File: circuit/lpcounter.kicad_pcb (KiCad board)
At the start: 2 copper layers, 58.4 x 40.6 mm, 17 parts, among them IC1 ATTINY85V-P, M1 SYN115, P1 CONN_01X08

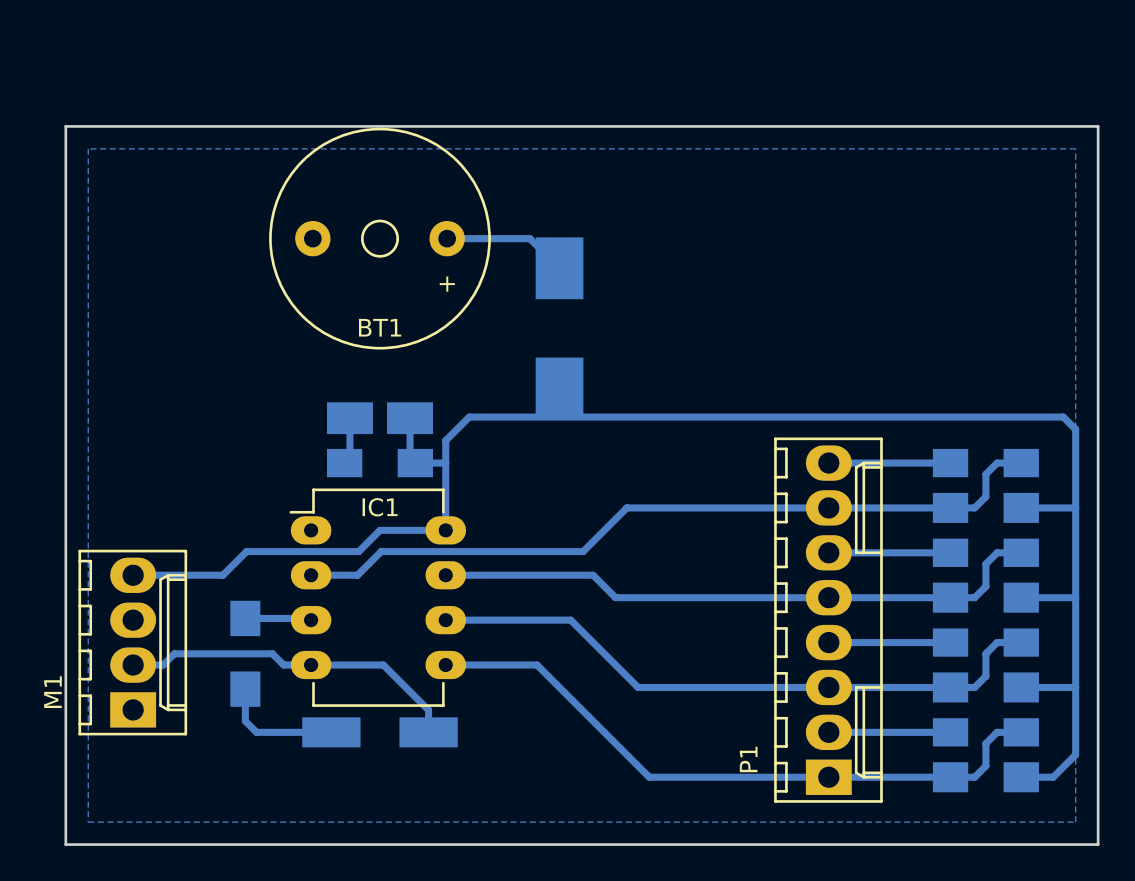
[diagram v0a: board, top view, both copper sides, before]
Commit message: proper battery holder for CR2032
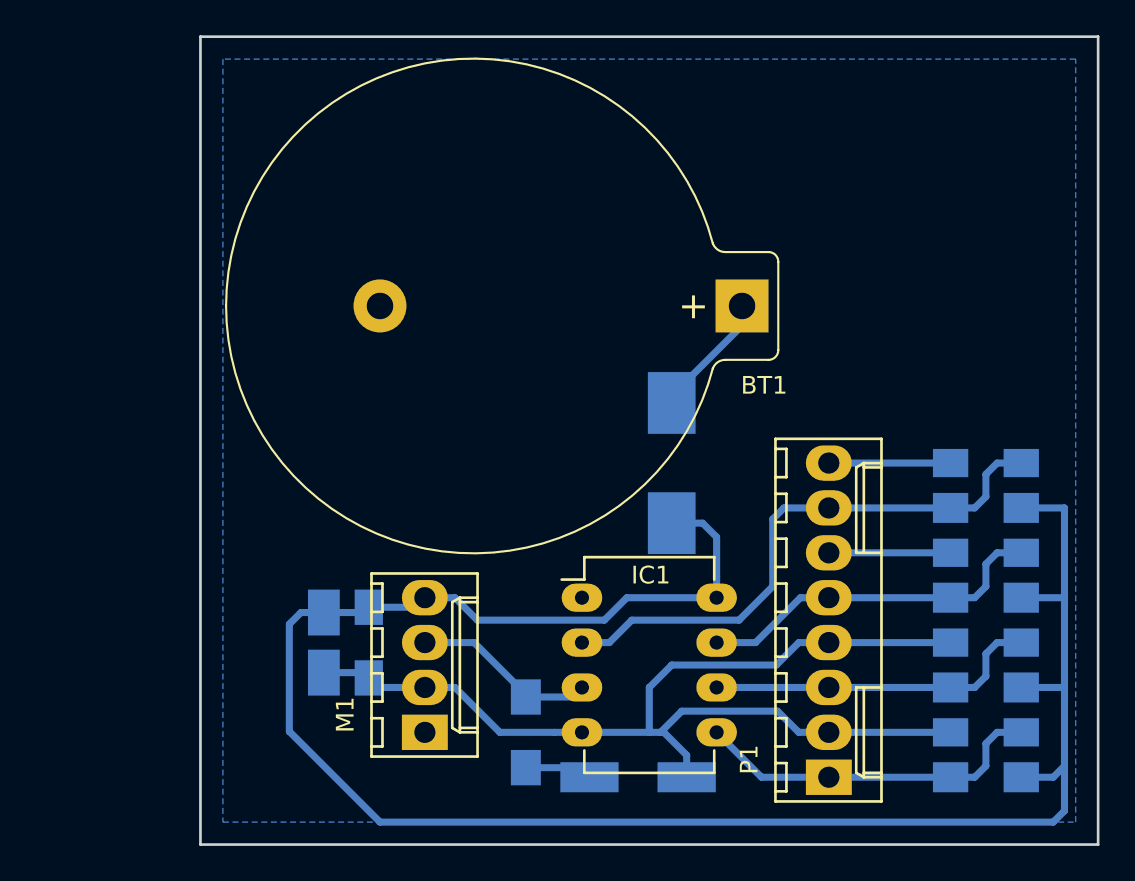
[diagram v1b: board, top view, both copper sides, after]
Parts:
- BT1: footprint Buzzers_Beepers:Buzzer_12x9.5RM7.6 -> Battery_Holders:Keystone_106_1x20mm-CoinCell
- moved BT1 20.8 mm to (172.9, 35.6)
- moved M1 16.6 mm to (154.9, 59.7)
- moved R5 16.5 mm to (160.7, 59.7)
- moved IC1 15.8 mm to (163.8, 52.1)
- moved D2 14.8 mm to (167.0, 62.2)
- moved C5 13.1 mm to (149.2, 54.6), turned to 270 degrees
- moved C6 10.2 mm to (151.8, 54.6), turned to 270 degrees
- moved D1 9.92 mm to (168.9, 44.5)
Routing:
- net GND: track 49.8 -> 75.5 mm
- net /IN0: track 37.0 -> 20.1 mm
- net /IN1: track 35.9 -> 19.0 mm
- net +3V3: track 96.0 -> 112.1 mm
- net /IN2: track 34.9 -> 20.1 mm
- net /IN3: track 43.6 -> 32.0 mm
- net /OUT: track 3.76 -> 10.5 mm
- net /LED: track 6.94 -> 3.82 mm
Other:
- board size 58.4 x 40.6 mm -> 50.8 x 45.7 mm

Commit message: updating PCB
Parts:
- M1: footprint Connectors_Molex:Molex_KK-6410-04_04x2.54mm_Straight -> Pin_Headers:Pin_Header_Straight_1x04_Pitch2.00mm
- moved M1 1.08 mm to (154.9, 58.6), turned to 180 degrees
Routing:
- net +3V3: track 112.1 -> 111.4 mm

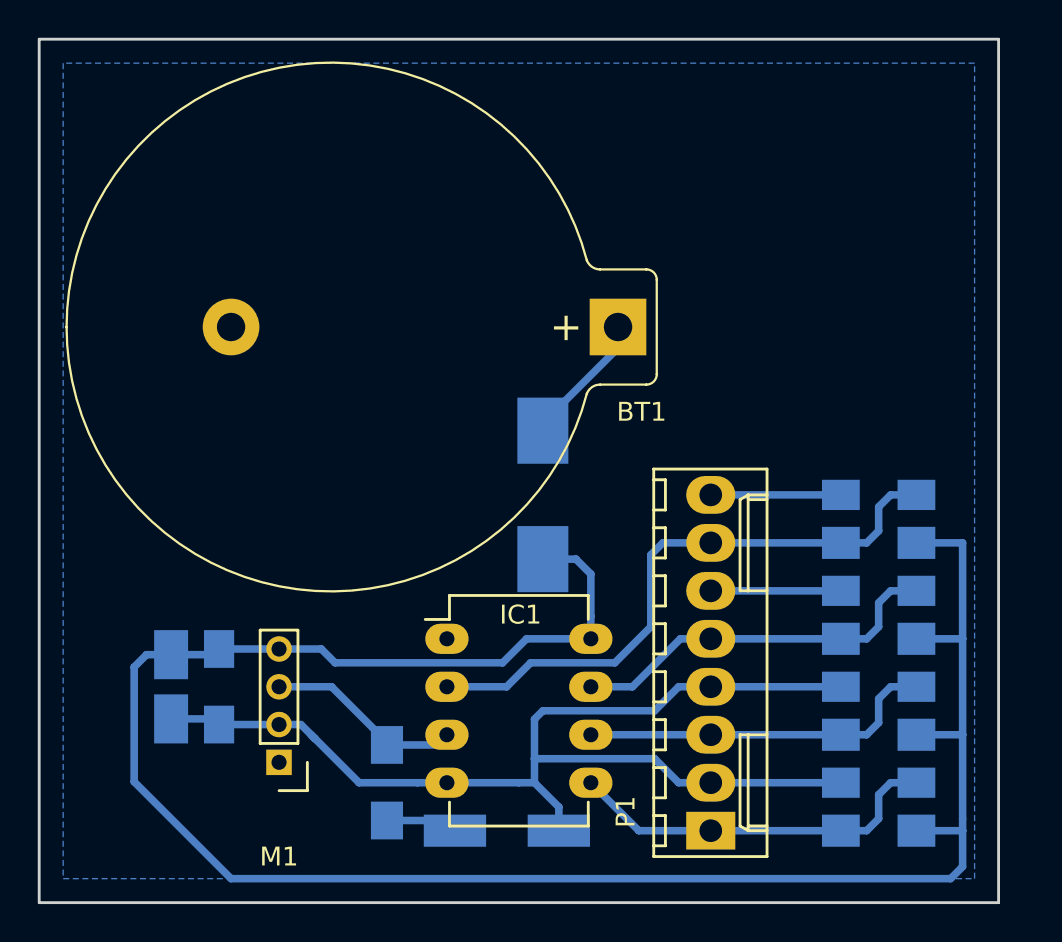
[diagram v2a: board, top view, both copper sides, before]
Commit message: fully routed
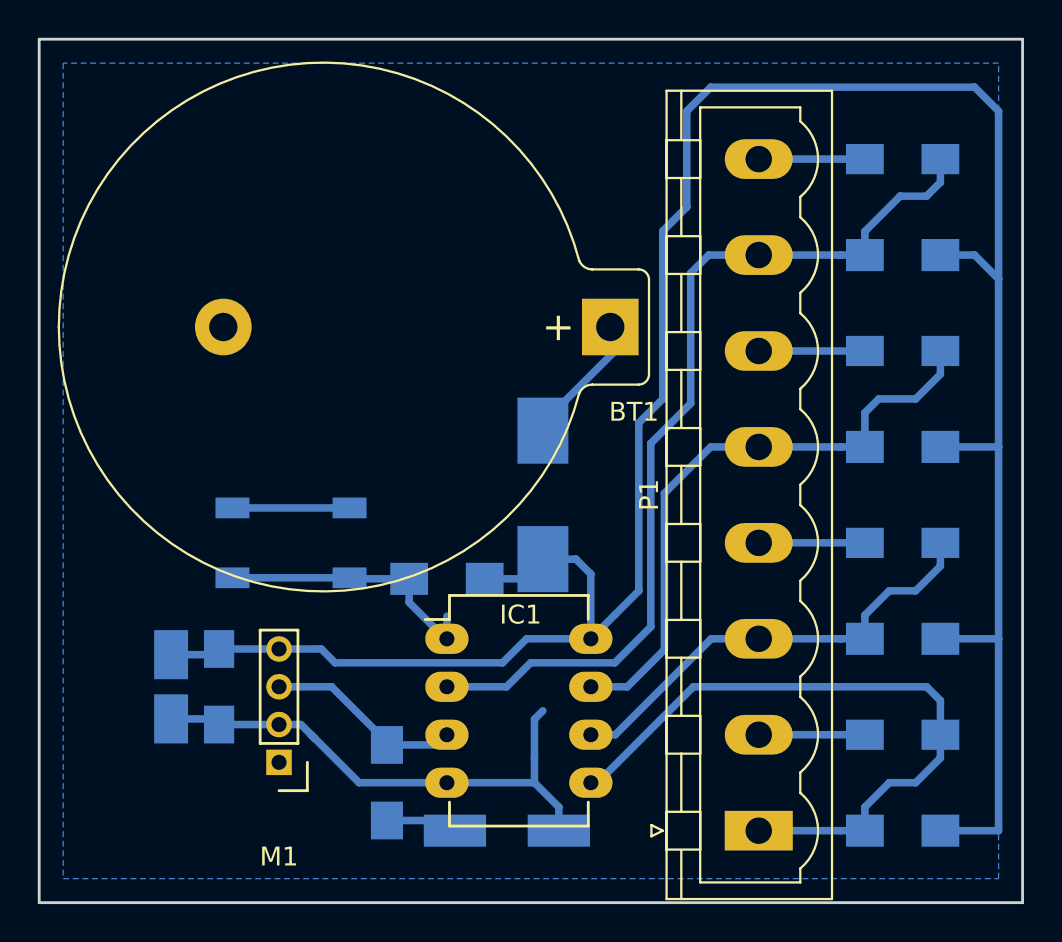
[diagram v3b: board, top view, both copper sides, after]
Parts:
- added P2: CONN_02X01, Buttons_Switches_SMD:SW_SPST_SKQG, B.Cu at (155.6, 47.0)
- added R6: 10k, Resistors_SMD:R_1206_HandSoldering, B.Cu at (163.8, 48.9)
- P1: footprint Connectors_Molex:Molex_KK-6410-08_08x2.54mm_Straight -> Connectors_Phoenix:PhoenixContact_MSTBVA-G_08x5.08mm_Vertical
- moved C4 17.8 mm to (188.0, 26.7)
- moved R4 15.3 mm to (188.0, 31.8)
- moved C3 12.8 mm to (188.0, 36.8)
- moved R3 10.2 mm to (188.0, 41.9)
- moved C2 7.73 mm to (188.0, 47.0)
- moved R2 5.24 mm to (188.0, 52.1)
- moved C1 2.84 mm to (188.0, 57.1)
- moved P1 2.54 mm to (180.3, 62.2)
- moved R1 1.27 mm to (188.0, 62.2)
- moved BT1 0.41 mm to (172.5, 35.6)
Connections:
- IC1 pad 1: (no net) -> /RESETn
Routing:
- net +3V3: track 111.4 -> 131.9 mm
- net GND: track 75.6 -> 57.4 mm
- net /IN3: track 32.0 -> 49.0 mm
- net /IN0: track 20.1 -> 36.1 mm
- net /RESETn: track 0.00 -> 14.6 mm
- net /IN2: track 20.1 -> 32.7 mm
- net /IN1: track 19.0 -> 24.3 mm
- net Net-(BT1-Pad1): track 7.14 -> 7.86 mm
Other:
- board size 50.8 x 45.7 mm -> 52.1 x 45.7 mm

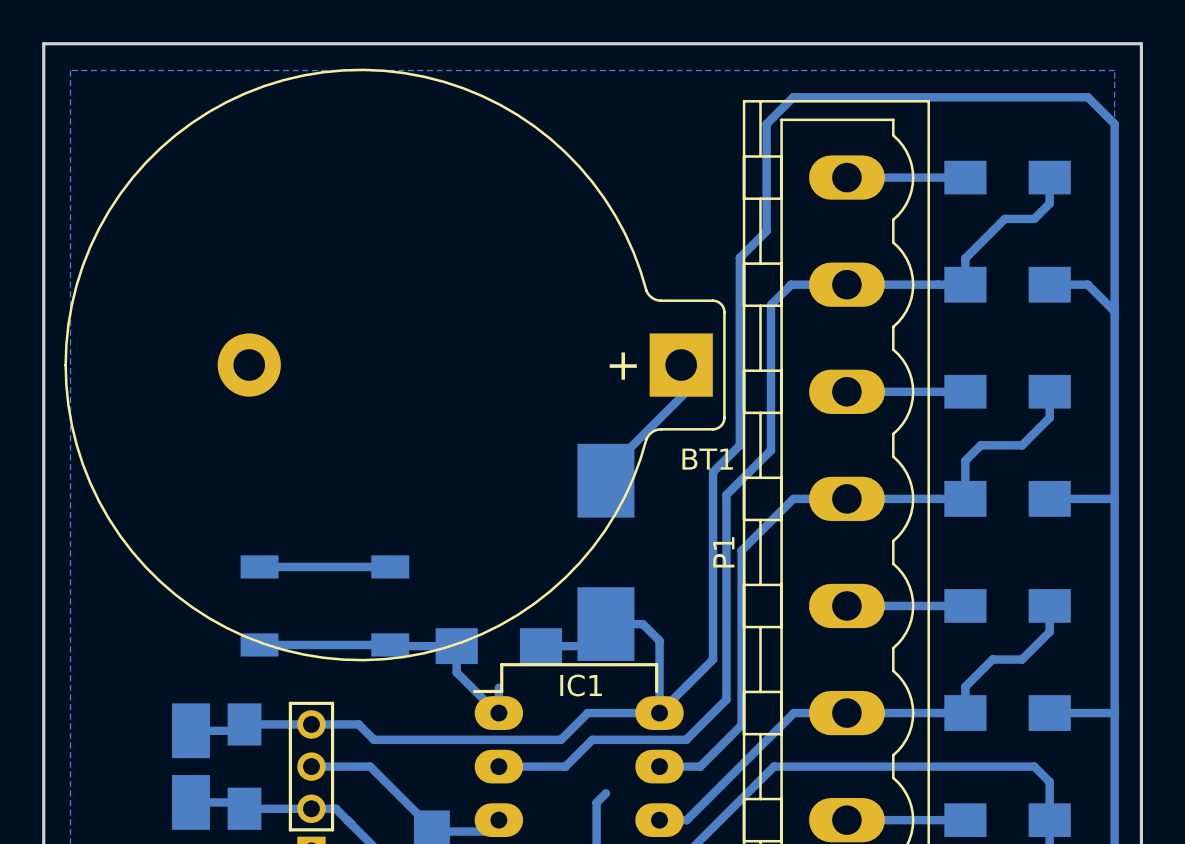
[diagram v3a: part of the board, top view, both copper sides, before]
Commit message: small chamges, optimizing routes
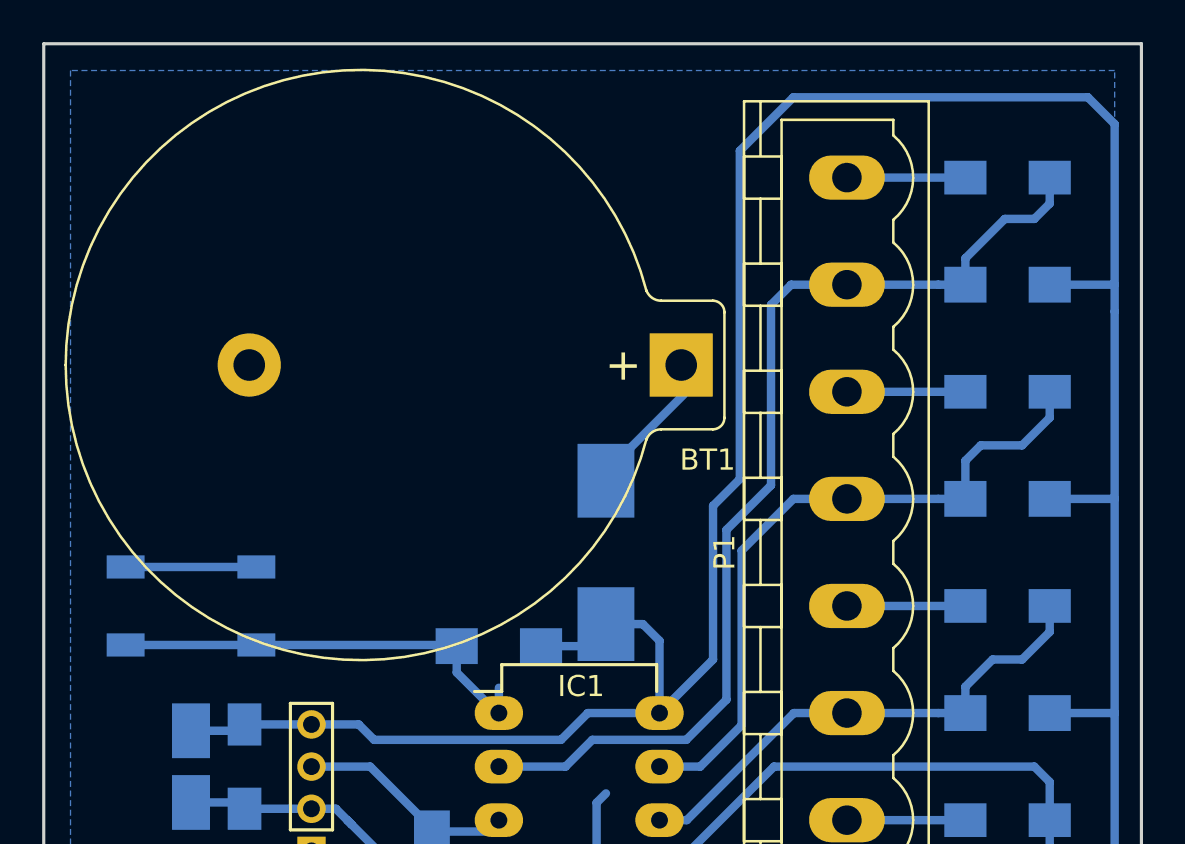
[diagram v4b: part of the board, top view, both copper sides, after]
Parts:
- moved P2 6.35 mm to (149.2, 47.0)
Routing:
- net /RESETn: track 14.6 -> 21.1 mm
- net +3V3: track 131.9 -> 131.4 mm
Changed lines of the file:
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@@
     (links 43)
     (no_connects 0)
-    (area 142.164999 20.244999 193.115001 66.115001)
+    (area 142.164999 20.244999 194.385001 66.115001)
     (thickness 1.6)
     (drawings 4)
-    (tracks 132)
+    (tracks 129)
     (zones 0)
     (modules 19)
@@
   )
   (module Buttons_Switches_SMD:SW_SPST_SKQG (layer B.Cu)
-    (at 155.575 46.99 180)
+    (at 149.225 46.99 180)
     (descr "ALPS 5.2mm Square Low-profile TACT Switch (SMD)")
     (tags "SPST Button Switch")
@@
   (segment (start 180.34 36.83) (end 185.96 36.83) (width 0.4) (layer B.Cu) (net 2))
   (segment (start 180.34 26.67) (end 185.96 26.67) (width 0.4) (layer B.Cu) (net 2))
-  (segment (start 152.475 45.14) (end 158.675 45.14) (width 0.4) (layer B.Cu) (net 2))
+  (segment (start 146.125 45.14) (end 152.325 45.14) (width 0.4) (layer B.Cu) (net 2))
   (segment (start 168.465 59.69) (end 168.465 58.42) (width 0.4) (layer B.Cu) (net 2))
   (segment (start 168.465 56.3246) (end 168.91 55.88) (width 0.4) (layer B.Cu) (net 2))
@@
   (segment (start 163.83 54.61) (end 166.992 54.61) (width 0.4) (layer B.Cu) (net 6))
   (segment (start 166.992 54.61) (end 168.262 53.34) (width 0.4) (layer B.Cu) (net 6))
+  (segment (start 174.625 51.435) (end 174.625 43.380626) (width 0.4) (layer B.Cu) (net 6))
   (segment (start 168.262 53.34) (end 172.72 53.34) (width 0.4) (layer B.Cu) (net 6))
   (segment (start 172.72 53.34) (end 174.625 51.435) (width 0.4) (layer B.Cu) (net 6))
-  (segment (start 174.625 51.435) (end 174.625 41.721139) (width 0.4) (layer B.Cu) (net 6))
-  (segment (start 174.625 41.721139) (end 176.738663 39.607476) (width 0.4) (layer B.Cu) (net 6))
-  (segment (start 176.738663 39.607476) (end 176.738663 32.705388) (width 0.4) (layer B.Cu) (net 6))
+  (segment (start 176.738663 41.266963) (end 176.738663 32.705388) (width 0.4) (layer B.Cu) (net 6))
+  (segment (start 174.625 43.380626) (end 176.738663 41.266963) (width 0.4) (layer B.Cu) (net 6))
   (segment (start 176.738663 32.705388) (end 177.694051 31.75) (width 0.4) (layer B.Cu) (net 6))
   (segment (start 177.694051 31.75) (end 180.34 31.75) (width 0.4) (layer B.Cu) (net 6))
@@
   (segment (start 180.34 31.75) (end 184.67 31.75) (width 0.4) (layer B.Cu) (net 6))
   (segment (start 184.67 31.75) (end 185.96 31.75) (width 0.4) (layer B.Cu) (net 6))
-  (segment (start 193.04 24.13) (end 193.04 33.02) (width 0.4) (layer B.Cu) (net 7))
+  (segment (start 193.04 24.13) (end 193.04 31.75) (width 0.4) (layer B.Cu) (net 7))
+  (segment (start 193.04 31.75) (end 193.04 33.02) (width 0.4) (layer B.Cu) (net 7))
+  (segment (start 189.96 31.75) (end 193.04 31.75) (width 0.4) (layer B.Cu) (net 7))
+  (segment (start 171.45 52.07) (end 173.99 49.53) (width 0.4) (layer B.Cu) (net 7))
+  (segment (start 173.99 49.53) (end 173.99 42.239799) (width 0.4) (layer B.Cu) (net 7))
+  (segment (start 173.99 42.239799) (end 175.26 40.969799) (width 0.4) (layer B.Cu) (net 7))
+  (segment (start 175.26 40.969799) (end 175.26 25.4) (width 0.4) (layer B.Cu) (net 7))
+  (segment (start 177.8 22.86) (end 191.77 22.86) (width 0.4) (layer B.Cu) (net 7))
+  (segment (start 175.26 25.4) (end 177.8 22.86) (width 0.4) (layer B.Cu) (net 7))
   (segment (start 191.77 22.86) (end 193.04 24.13) (width 0.4) (layer B.Cu) (net 7))
-  (segment (start 177.8 22.86) (end 191.77 22.86) (width 0.4) (layer B.Cu) (net 7))
-  (segment (start 176.53 24.13) (end 177.8 22.86) (width 0.4) (layer B.Cu) (net 7))
-  (segment (start 176.53 27.679377) (end 176.53 24.13) (width 0.4) (layer B.Cu) (net 7))
-  (segment (start 176.53 29.21) (end 176.53 27.679377) (width 0.4) (layer B.Cu) (net 7))
-  (segment (start 175.26 30.48) (end 176.53 29.21) (width 0.4) (layer B.Cu) (net 7))
-  (segment (start 175.26 39.37) (end 175.26 30.48) (width 0.4) (layer B.Cu) (net 7))
-  (segment (start 173.99 40.64) (end 175.26 39.37) (width 0.4) (layer B.Cu) (net 7))
-  (segment (start 173.99 49.53) (end 173.99 40.64) (width 0.4) (layer B.Cu) (net 7))
-  (segment (start 172.72 50.8) (end 173.99 49.53) (width 0.4) (layer B.Cu) (net 7))
-  (segment (start 171.45 52.07) (end 172.72 50.8) (width 0.4) (layer B.Cu) (net 7))
   (segment (start 193.04 62.23) (end 193.04 52.07) (width 0.4) (layer B.Cu) (net 7))
   (segment (start 193.04 52.07) (end 193.04 41.91) (width 0.4) (layer B.Cu) (net 7))
@@
   (segment (start 193.04 41.91) (end 193.04 33.02) (width 0.4) (layer B.Cu) (net 7))
   (segment (start 189.96 41.91) (end 193.04 41.91) (width 0.4) (layer B.Cu) (net 7))
-  (segment (start 191.77 31.75) (end 189.96 31.75) (width 0.4) (layer B.Cu) (net 7))
-  (segment (start 193.04 33.02) (end 191.77 31.75) (width 0.4) (layer B.Cu) (net 7))
   (segment (start 167.866 48.895) (end 168.91 47.8511) (width 0.4) (layer B.Cu) (net 7))
   (segment (start 165.83 48.895) (end 167.866 48.895) (width 0.4) (layer B.Cu) (net 7))
@@
   (segment (start 163.29 57.69) (end 163.83 57.15) (width 0.4) (layer B.Cu) (net 9))
   (segment (start 160.655 57.69) (end 163.29 57.69) (width 0.4) (layer B.Cu) (net 9))
-  (segment (start 158.675 48.84) (end 152.475 48.84) (width 0.4) (layer B.Cu) (net 10))
-  (segment (start 158.73 48.895) (end 158.675 48.84) (width 0.4) (layer B.Cu) (net 10))
-  (segment (start 161.83 48.895) (end 158.73 48.895) (width 0.4) (layer B.Cu) (net 10))
+  (segment (start 152.325 48.84) (end 161.775 48.84) (width 0.4) (layer B.Cu) (net 10))
+  (segment (start 161.775 48.84) (end 161.83 48.895) (width 0.4) (layer B.Cu) (net 10))
+  (segment (start 152.325 48.84) (end 146.125 48.84) (width 0.4) (layer B.Cu) (net 10))
+  (segment (start 152.38 48.895) (end 152.325 48.84) (width 0.4) (layer B.Cu) (net 10))
   (segment (start 163.755 52.07) (end 163.83 52.07) (width 0.4) (layer B.Cu) (net 10))
   (segment (start 161.83 50.145) (end 163.755 52.07) (width 0.4) (layer B.Cu) (net 10))
